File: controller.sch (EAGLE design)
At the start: 7 parts, among them U1 ATMEGA328P_PDIP

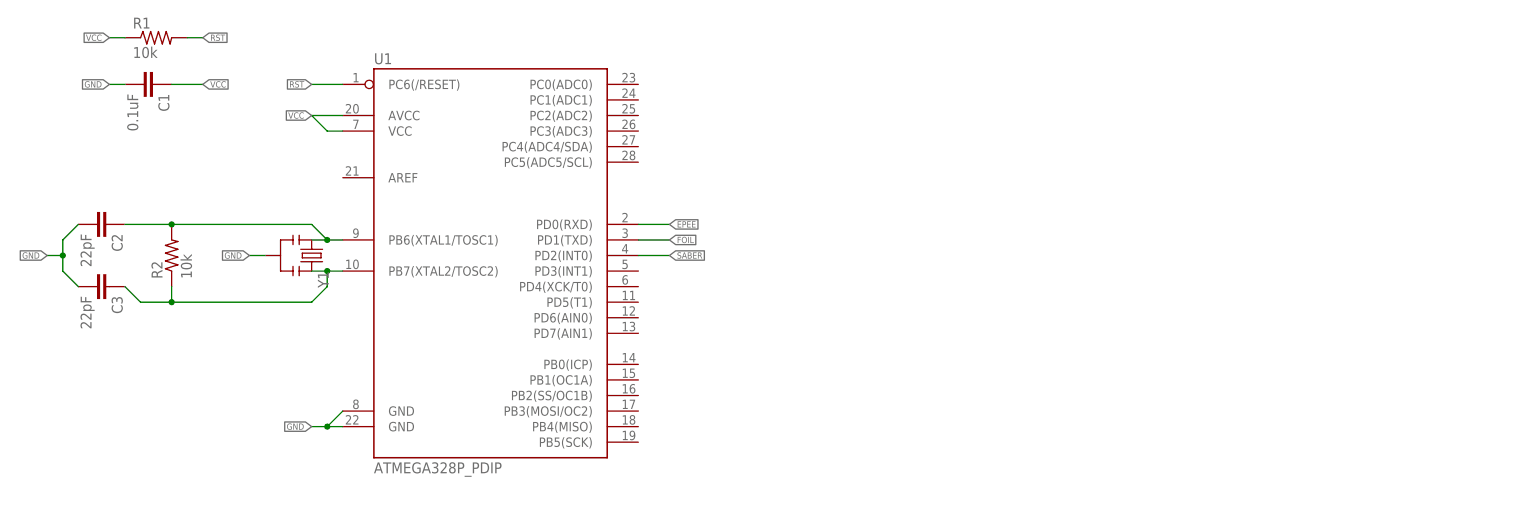
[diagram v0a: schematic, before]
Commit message: Added gitignroe file. Finished layout out board.
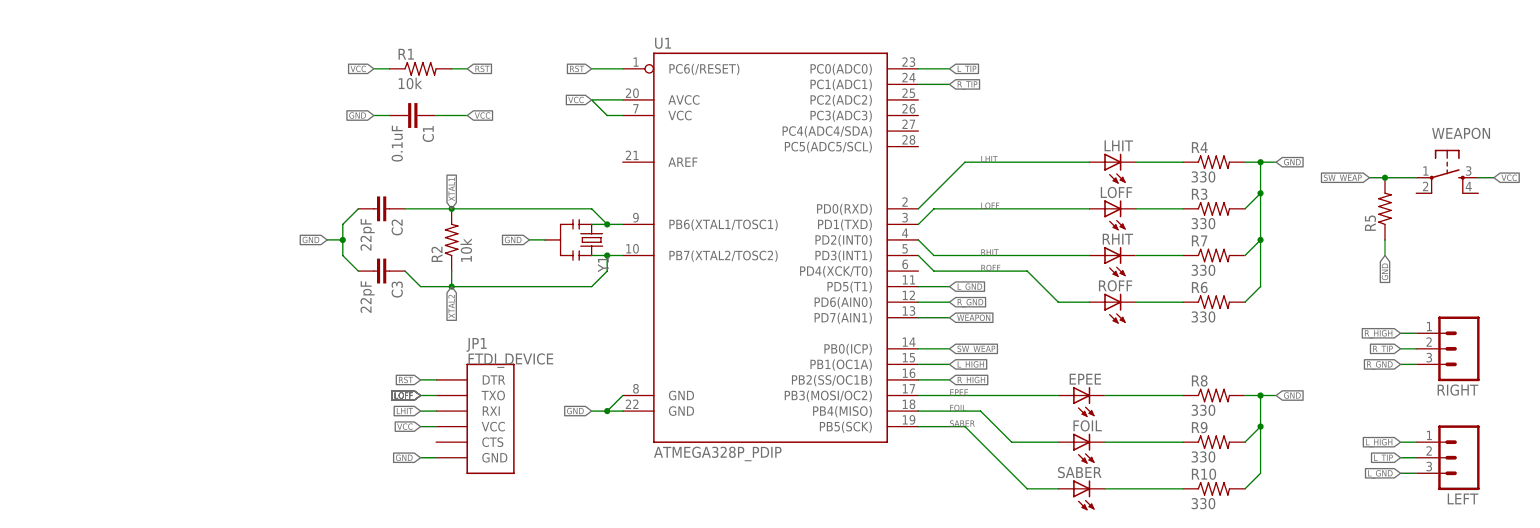
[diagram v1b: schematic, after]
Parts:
- added EPEE, FOIL, LHIT, LOFF, RHIT, ROFF, SABER: (no value), SparkFun-LED:LED5MM
- added JP1: FTDI_DEVICE, SparkFun-Connectors:FTDI_DEVICE
- added LEFT, RIGHT: (no value), SparkFun-Connectors:M03LOCK_LONGPADS
- added R10, R3, R4, R6, R7, R8, R9: 330, SparkFun-Resistors:RESISTOR0603-RES
- added R5: (no value), SparkFun-Resistors:RESISTORPTH-1/4W
- added WEAPON: (no value), SparkFun-Electromechanical:TAC_SWITCHPTH
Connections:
- net N$2 renamed XTAL1
- net N$4 renamed XTAL2
- new net LHIT: JP1.RXI, LHIT.A, U1.PD0(RXD)
- new net LOFF: JP1.TXO, LOFF.A, U1.PD1(TXD)
- new net L_GND: LEFT.3, U1.PD5(T1)
- new net L_HIGH: LEFT.1, U1.PB1(OC1A)
- new net L_TIP: LEFT.2, U1.PC0(ADC0)
- new net N$1: LHIT.C, R4.1
- new net N$2: LOFF.C, R3.1
- new net N$3: R7.1, RHIT.C
- new net N$4: R6.1, ROFF.C
- new net N$5: FOIL.C, R9.1
- new net N$6: R10.1, SABER.C
- new net N$8: EPEE.C, R8.1
- new net RHIT: RHIT.A, U1.PD2(INT0)
- new net ROFF: ROFF.A, U1.PD3(INT1)
- new net R_GND: RIGHT.3, U1.PD6(AIN0)
- new net R_HIGH: RIGHT.1, U1.PB2(SS/OC1B)
- new net R_TIP: RIGHT.2, U1.PC1(ADC1)
- new net SW_WEAP: R5.2, U1.PB0(ICP), WEAPON.1
- new net WEAPON: U1.PD7(AIN1)
- net EPEE: now also EPEE.A, U1.PB3(MOSI/OC2); no longer U1.PD0(RXD)
- net FOIL: now also FOIL.A, U1.PB4(MISO); no longer U1.PD1(TXD)
- net GND: now also JP1.GND, R10.2, R3.2, R4.2, R5.1, R6.2, R7.2, R8.2, R9.2
- net RST: now also JP1.DTR
- net SABER: now also SABER.A, U1.PB5(SCK); no longer U1.PD2(INT0)
- net VCC: now also JP1.VCC, WEAPON.3
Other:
- moved on the sheet: C1, C2, C3, R1, R2, U1, Y1

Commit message: Fixed part values and modified silkscreen
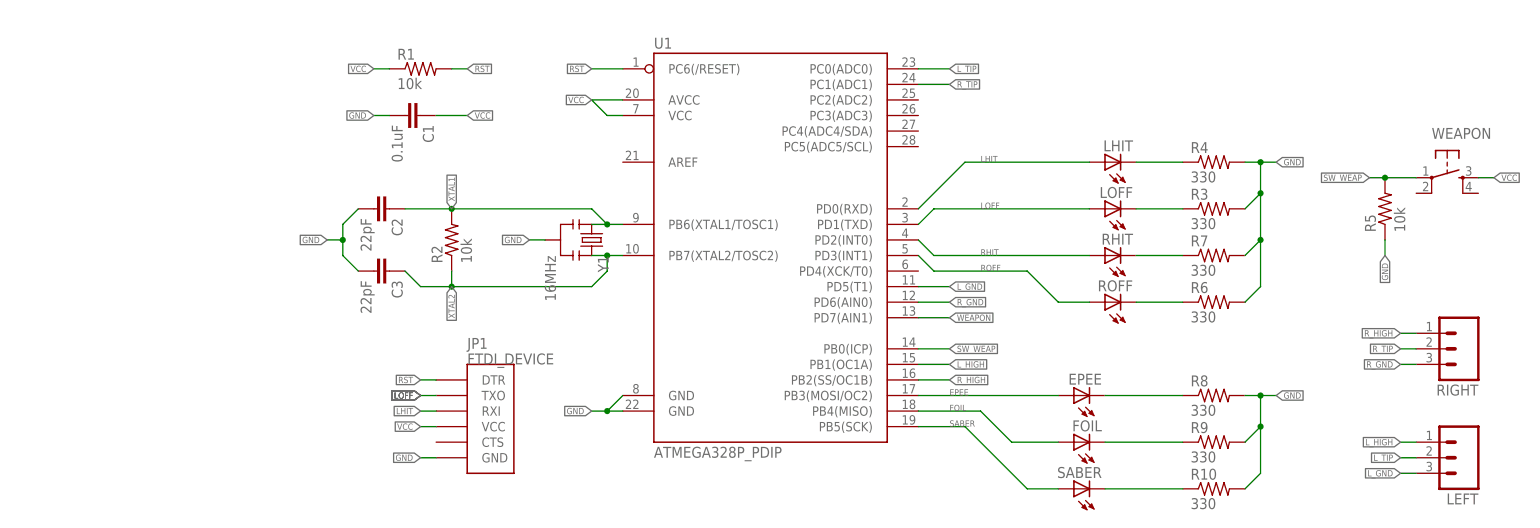
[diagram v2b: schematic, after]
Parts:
- R5: value (none) -> 10k
- Y1: value (none) -> 16MHz
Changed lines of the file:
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@@
 <part name="R1" library="SparkFun-Resistors" deviceset="RESISTOR" device="PTH-1/4W" value="10k"/>
 <part name="R2" library="SparkFun-Resistors" deviceset="RESISTOR" device="PTH-1/4W" value="10k"/>
-<part name="Y1" library="SparkFun-FreqCtrl" deviceset="RESONATOR" device="PTH"/>
+<part name="Y1" library="SparkFun-FreqCtrl" deviceset="RESONATOR" device="PTH" value="16MHz"/>
 <part name="C2" library="SparkFun-Capacitors" deviceset="CAP" device="KIT" value="22pF"/>
 <part name="C3" library="SparkFun-Capacitors" deviceset="CAP" device="KIT" value="22pF"/>
@@
 <part name="SABER" library="SparkFun-LED" deviceset="LED" device="5MM"/>
 <part name="WEAPON" library="SparkFun-Electromechanical" deviceset="TAC_SWITCH" device="PTH"/>
-<part name="R5" library="SparkFun-Resistors" deviceset="RESISTOR" device="PTH-1/4W"/>
+<part name="R5" library="SparkFun-Resistors" deviceset="RESISTOR" device="PTH-1/4W" value="10k"/>
 <part name="JP1" library="SparkFun-Connectors" deviceset="FTDI_DEVICE" device=""/>
 <part name="R6" library="SparkFun-Resistors" deviceset="RESISTOR" device="0603-RES" value="330"/>

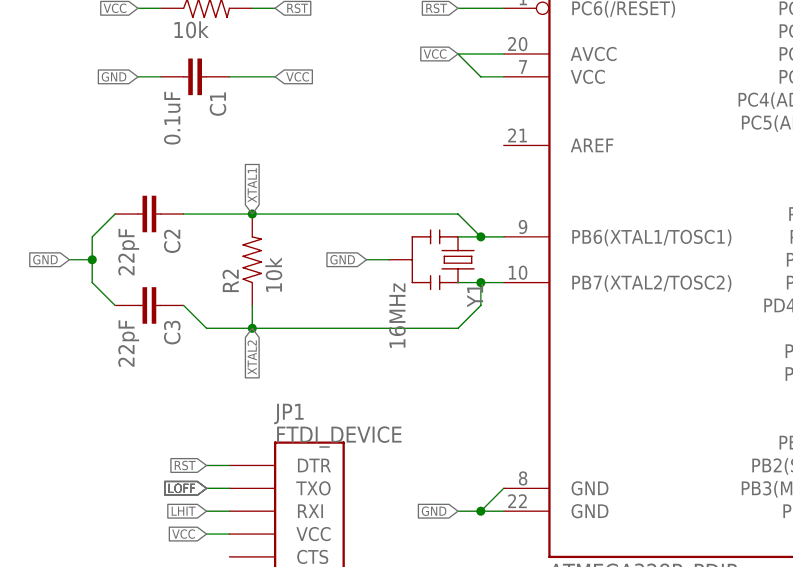
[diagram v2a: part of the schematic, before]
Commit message: Replaced resonator with crystal and updated CAM job
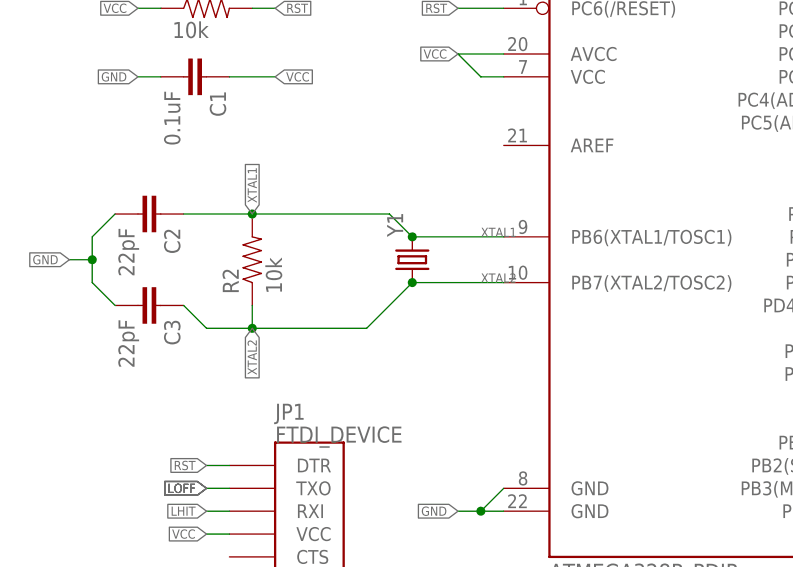
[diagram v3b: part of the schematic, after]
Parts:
- Y1: value 16MHz -> (none); device SparkFun-FreqCtrl:RESONATORPTH -> SparkFun-FreqCtrl:CRYSTALHC49US
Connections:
- net GND: no longer Y1.2
- net XTAL1: now also Y1.2; no longer Y1.1
- net XTAL2: now also Y1.1; no longer Y1.3
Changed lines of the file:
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@@
 <part name="R1" library="SparkFun-Resistors" deviceset="RESISTOR" device="PTH-1/4W" value="10k"/>
 <part name="R2" library="SparkFun-Resistors" deviceset="RESISTOR" device="PTH-1/4W" value="10k"/>
-<part name="Y1" library="SparkFun-FreqCtrl" deviceset="RESONATOR" device="PTH" value="16MHz"/>
 <part name="C2" library="SparkFun-Capacitors" deviceset="CAP" device="KIT" value="22pF"/>
 <part name="C3" library="SparkFun-Capacitors" deviceset="CAP" device="KIT" value="22pF"/>
@@
 <part name="LEFT" library="SparkFun-Connectors" deviceset="M03" device="LOCK_LONGPADS"/>
 <part name="RIGHT" library="SparkFun-Connectors" deviceset="M03" device="LOCK_LONGPADS"/>
+<part name="Y1" library="SparkFun-FreqCtrl" deviceset="CRYSTAL" device="HC49US"/>
 </parts>
 <sheets>
@@
 <instance part="R1" gate="G$1" x="22.86" y="73.66"/>
 <instance part="R2" gate="G$1" x="27.94" y="45.72" rot="R90"/>
-<instance part="Y1" gate="G$1" x="50.8" y="45.72" rot="R270"/>
 <instance part="C2" gate="G$1" x="15.24" y="50.8" rot="R270"/>
 <instance part="C3" gate="G$1" x="15.24" y="40.64" rot="R270"/>
@@
 <instance part="LEFT" gate="G$1" x="193.04" y="10.16" rot="R180"/>
 <instance part="RIGHT" gate="G$1" x="193.04" y="27.94" rot="R180"/>
+<instance part="Y1" gate="G$1" x="45.72" y="45.72" rot="R90"/>
 </instances>
 <busses>
@@
 <junction x="10.16" y="45.72"/>
 <label x="7.62" y="45.72" size="1.016" layer="95" rot="R180" xref="yes"/>
-</segment>
-<segment>
-<pinref part="Y1" gate="G$1" pin="2"/>
-<wire x1="43.18" y1="45.72" x2="40.64" y2="45.72" width="0.1524" layer="91"/>
-<label x="40.64" y="45.72" size="1.016" layer="95" rot="R180" xref="yes"/>
 </segment>
 <segment>
@@
 </segment>
 </net>
-<net name="XTAL1" class="0">
-<segment>
-<pinref part="U1" gate="G$1" pin="PB6(XTAL1/TOSC1)"/>
-<pinref part="Y1" gate="G$1" pin="1"/>
-<wire x1="55.88" y1="48.26" x2="53.34" y2="48.26" width="0.1524" layer="91"/>
-<wire x1="53.34" y1="48.26" x2="50.8" y2="48.26" width="0.1524" layer="91"/>
-<wire x1="53.34" y1="48.26" x2="50.8" y2="50.8" width="0.1524" layer="91"/>
-<junction x="53.34" y="48.26"/>
-<pinref part="C2" gate="G$1" pin="1"/>
-<pinref part="R2" gate="G$1" pin="2"/>
-<wire x1="20.32" y1="50.8" x2="27.94" y2="50.8" width="0.1524" layer="91"/>
-<wire x1="50.8" y1="50.8" x2="27.94" y2="50.8" width="0.1524" layer="91"/>
-<junction x="27.94" y="50.8"/>
-<label x="27.94" y="50.8" size="1.016" layer="95" rot="R90" xref="yes"/>
-</segment>
-</net>
-<net name="XTAL2" class="0">
-<segment>
-<pinref part="U1" gate="G$1" pin="PB7(XTAL2/TOSC2)"/>
-<pinref part="Y1" gate="G$1" pin="3"/>
-<wire x1="55.88" y1="43.18" x2="53.34" y2="43.18" width="0.1524" layer="91"/>
-<wire x1="53.34" y1="43.18" x2="50.8" y2="43.18" width="0.1524" layer="91"/>
-<wire x1="53.34" y1="43.18" x2="53.34" y2="40.64" width="0.1524" layer="91"/>
-<wire x1="53.34" y1="40.64" x2="50.8" y2="38.1" width="0.1524" layer="91"/>
-<junction x="53.34" y="43.18"/>
-<pinref part="R2" gate="G$1" pin="1"/>
-<pinref part="C3" gate="G$1" pin="1"/>
-<wire x1="22.86" y1="38.1" x2="20.32" y2="40.64" width="0.1524" layer="91"/>
-<wire x1="50.8" y1="38.1" x2="27.94" y2="38.1" width="0.1524" layer="91"/>
-<wire x1="27.94" y1="38.1" x2="22.86" y2="38.1" width="0.1524" layer="91"/>
-<wire x1="27.94" y1="40.64" x2="27.94" y2="38.1" width="0.1524" layer="91"/>
-<junction x="27.94" y="38.1"/>
-<label x="27.94" y="38.1" size="1.016" layer="95" rot="R270" xref="yes"/>
-</segment>
-</net>
 <net name="L_GND" class="0">
 <segment>
@@
 </segment>
 </net>
+<net name="XTAL1" class="0">
+<segment>
+<pinref part="Y1" gate="G$1" pin="2"/>
+<pinref part="U1" gate="G$1" pin="PB6(XTAL1/TOSC1)"/>
+<wire x1="45.72" y1="48.26" x2="55.88" y2="48.26" width="0.1524" layer="91"/>
+<pinref part="R2" gate="G$1" pin="2"/>
+<pinref part="C2" gate="G$1" pin="1"/>
+<wire x1="20.32" y1="50.8" x2="27.94" y2="50.8" width="0.1524" layer="91"/>
+<label x="27.94" y="50.8" size="1.016" layer="95" rot="R90" xref="yes"/>
+<wire x1="45.72" y1="48.26" x2="43.18" y2="50.8" width="0.1524" layer="91"/>
+<wire x1="43.18" y1="50.8" x2="27.94" y2="50.8" width="0.1524" layer="91"/>
+<junction x="45.72" y="48.26"/>
+<junction x="27.94" y="50.8"/>
+<label x="53.34" y="48.26" size="1.016" layer="95"/>
+</segment>
+</net>
+<net name="XTAL2" class="0">
+<segment>
+<pinref part="U1" gate="G$1" pin="PB7(XTAL2/TOSC2)"/>
+<pinref part="Y1" gate="G$1" pin="1"/>
+<wire x1="55.88" y1="43.18" x2="45.72" y2="43.18" width="0.1524" layer="91"/>
+<wire x1="45.72" y1="43.18" x2="40.64" y2="38.1" width="0.1524" layer="91"/>
+<junction x="45.72" y="43.18"/>
+<pinref part="C3" gate="G$1" pin="1"/>
+<wire x1="22.86" y1="38.1" x2="20.32" y2="40.64" width="0.1524" layer="91"/>
+<pinref part="R2" gate="G$1" pin="1"/>
+<wire x1="27.94" y1="40.64" x2="27.94" y2="38.1" width="0.1524" layer="91"/>
+<wire x1="27.94" y1="38.1" x2="22.86" y2="38.1" width="0.1524" layer="91"/>
+<label x="27.94" y="38.1" size="1.016" layer="95" rot="R270" xref="yes"/>
+<wire x1="40.64" y1="38.1" x2="27.94" y2="38.1" width="0.1524" layer="91"/>
+<junction x="27.94" y="38.1"/>
+<label x="53.34" y="43.18" size="1.016" layer="95"/>
+</segment>
+</net>
